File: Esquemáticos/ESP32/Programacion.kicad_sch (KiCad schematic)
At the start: 13 parts, among them J4 USB Programador, U7 ESP32-WROOM-32

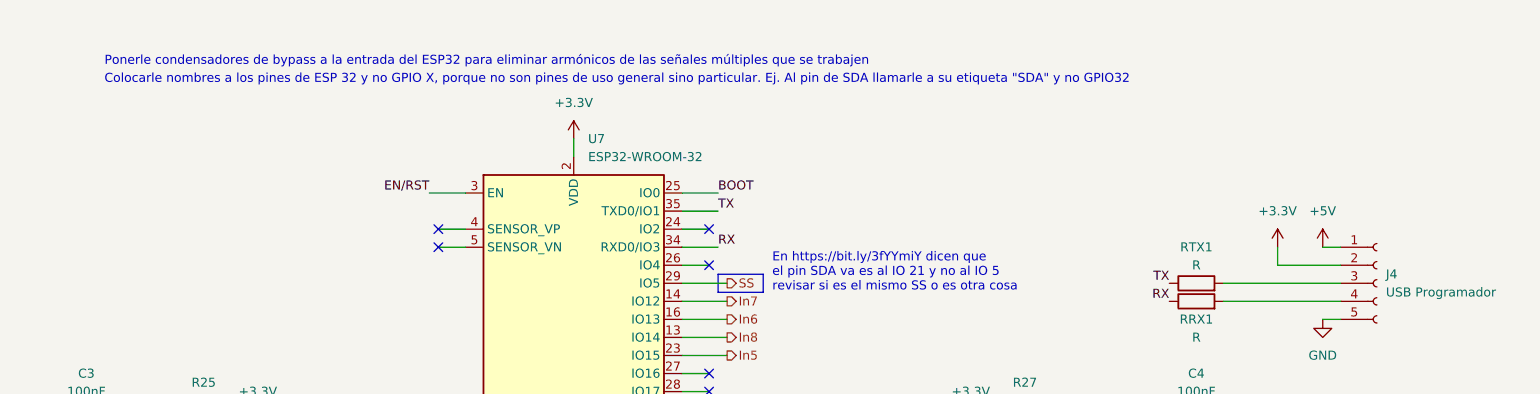
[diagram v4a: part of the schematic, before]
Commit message: Auxilio? Bypass 3.3V ESP32
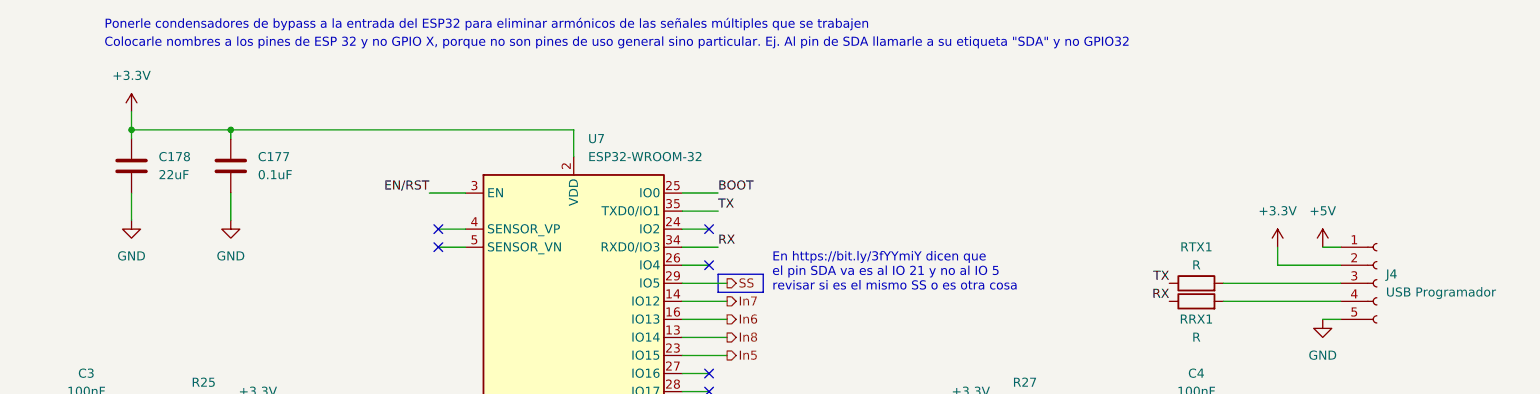
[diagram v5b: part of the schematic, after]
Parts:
- added C177: 0.1uF, Capacitor_SMD:C_0603_1608Metric_Pad1.08x0.95mm_HandSolder, symbol Device:C
- added C178: 22uF, Capacitor_SMD:C_0603_1608Metric_Pad1.08x0.95mm_HandSolder, symbol Device:C
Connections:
- net +3.3V: now also C177.1, C178.1
- net GND: now also C177.2, C178.2
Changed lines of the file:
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@@
   (junction (at 237.49 124.46) (diameter 0) (color 0 0 0 0)
   )
+  (junction (at 80.01 68.58) (diameter 0) (color 0 0 0 0)
+  )
   (junction (at 81.28 124.46) (diameter 0) (color 0 0 0 0)
   )
   (junction (at 66.04 124.46) (diameter 0) (color 0 0 0 0)
+  )
+  (junction (at 93.98 68.58) (diameter 0) (color 0 0 0 0)
   )
   (no_connect (at 123.19 120.65))
@@
     (stroke (width 0) (type default) (color 0 0 0 0))
   )
+  (wire (pts (xy 93.98 68.58) (xy 80.01 68.58))
+    (stroke (width 0) (type default) (color 0 0 0 0))
+  )
   (wire (pts (xy 161.29 133.35) (xy 157.48 133.35))
     (stroke (width 0) (type default) (color 0 0 0 0))
   )
+  (wire (pts (xy 142.24 72.39) (xy 142.24 68.58))
+    (stroke (width 0) (type default) (color 0 0 0 0))
+  )
   (wire (pts (xy 247.65 85.09) (xy 250.19 85.09))
     (stroke (width 0) (type default) (color 0 0 0 0))
@@
     (stroke (width 0) (type default) (color 0 0 0 0))
   )
-  (wire (pts (xy 142.24 69.85) (xy 142.24 72.39))
-    (stroke (width 0) (type default) (color 0 0 0 0))
-  )
   (wire (pts (xy 233.68 90.17) (xy 250.19 90.17))
     (stroke (width 0) (type default) (color 0 0 0 0))
@@
     (stroke (width 0) (type default) (color 0 0 0 0))
   )
+  (wire (pts (xy 80.01 68.58) (xy 80.01 69.85))
+    (stroke (width 0) (type default) (color 0 0 0 0))
+  )
   (wire (pts (xy 241.3 87.63) (xy 250.19 87.63))
     (stroke (width 0) (type default) (color 0 0 0 0))
@@
     (stroke (width 0) (type default) (color 0 0 0 0))
   )
+  (wire (pts (xy 93.98 68.58) (xy 93.98 69.85))
+    (stroke (width 0) (type default) (color 0 0 0 0))
+  )
   (wire (pts (xy 121.92 77.47) (xy 127 77.47))
     (stroke (width 0) (type default) (color 0 0 0 0))
@@
     (stroke (width 0) (type default) (color 0 0 0 0))
   )
+  (wire (pts (xy 80.01 77.47) (xy 80.01 81.28))
+    (stroke (width 0) (type default) (color 0 0 0 0))
+  )
   (wire (pts (xy 157.48 123.19) (xy 163.83 123.19))
     (stroke (width 0) (type default) (color 0 0 0 0))
@@
     (stroke (width 0) (type default) (color 0 0 0 0))
   )
+  (wire (pts (xy 93.98 77.47) (xy 93.98 81.28))
+    (stroke (width 0) (type default) (color 0 0 0 0))
+  )
   (wire (pts (xy 123.19 118.11) (xy 127 118.11))
     (stroke (width 0) (type default) (color 0 0 0 0))
@@
     (stroke (width 0) (type default) (color 0 0 0 0))
   )
+  (wire (pts (xy 142.24 68.58) (xy 93.98 68.58))
+    (stroke (width 0) (type default) (color 0 0 0 0))
+  )
   (wire (pts (xy 161.29 105.41) (xy 157.48 105.41))
     (stroke (width 0) (type default) (color 0 0 0 0))
@@
   )
   (wire (pts (xy 66.04 124.46) (xy 66.04 110.49))
+    (stroke (width 0) (type default) (color 0 0 0 0))
+  )
+  (wire (pts (xy 80.01 66.04) (xy 80.01 68.58))
     (stroke (width 0) (type default) (color 0 0 0 0))
   )
@@
   )
   (text "Ponerle condensadores de bypass a la entrada del ESP32 para eliminar armónicos de las señales múltiples que se trabajen\n"
-    (at 76.2 59.69 0)
+    (at 76.2 54.61 0)
     (effects (font (size 1.27 1.27)) (justify left bottom))
   )
@@
   )
   (text "Colocarle nombres a los pines de ESP 32 y no GPIO X, porque no son pines de uso general sino particular. Ej. Al pin de SDA llamarle a su etiqueta \"SDA\" y no GPIO32"
-    (at 76.2 62.23 0)
+    (at 76.2 57.15 0)
     (effects (font (size 1.27 1.27)) (justify left bottom))
   )
@@
     (pin "2")
   )
+  (symbol (lib_id "Device:C") (at 80.01 73.66 0) (mirror y) (unit 1)
+    (in_bom yes) (on_board yes) (fields_autoplaced)
+    (property "Reference" "C178" (id 0) (at 83.82 72.3899 0)
+      (effects (font (size 1.27 1.27)) (justify right))
+    )
+    (property "Value" "22uF" (id 1) (at 83.82 74.9299 0)
+      (effects (font (size 1.27 1.27)) (justify right))
+    )
+    (property "Footprint" "Capacitor_SMD:C_0603_1608Metric_Pad1.08x0.95mm_HandSolder" (id 2) (at 79.0448 77.47 0)
+      (effects (font (size 1.27 1.27)) hide)
+    )
+    (property "Datasheet" "~" (id 3) (at 80.01 73.66 0)
+      (effects (font (size 1.27 1.27)) hide)
+    )
+    (pin "1")
+    (pin "2")
+  )
   (symbol (lib_id "Device:R") (at 218.44 124.46 270) (mirror x) (unit 1)
     (in_bom yes) (on_board yes) (fields_autoplaced)
@@
     (pin "2")
   )
-  (symbol (lib_id "power:+3.3V") (at 142.24 69.85 0) (unit 1)
-    (in_bom yes) (on_board yes) (fields_autoplaced)
-    (property "Reference" "#PWR030" (id 0) (at 142.24 73.66 0)
-      (effects (font (size 1.27 1.27)) hide)
-    )
-    (property "Value" "+3.3V" (id 1) (at 142.24 64.77 0))
-    (property "Footprint" "" (id 2) (at 142.24 69.85 0)
-      (effects (font (size 1.27 1.27)) hide)
-    )
-    (property "Datasheet" "" (id 3) (at 142.24 69.85 0)
+  (symbol (lib_id "Device:C") (at 93.98 73.66 0) (mirror y) (unit 1)
+    (in_bom yes) (on_board yes) (fields_autoplaced)
+    (property "Reference" "C177" (id 0) (at 97.79 72.3899 0)
+      (effects (font (size 1.27 1.27)) (justify right))
+    )
+    (property "Value" "0.1uF" (id 1) (at 97.79 74.9299 0)
+      (effects (font (size 1.27 1.27)) (justify right))
+    )
+    (property "Footprint" "Capacitor_SMD:C_0603_1608Metric_Pad1.08x0.95mm_HandSolder" (id 2) (at 93.0148 77.47 0)
+      (effects (font (size 1.27 1.27)) hide)
+    )
+    (property "Datasheet" "~" (id 3) (at 93.98 73.66 0)
+      (effects (font (size 1.27 1.27)) hide)
+    )
+    (pin "1")
+    (pin "2")
+  )
+  (symbol (lib_id "power:+3.3V") (at 80.01 66.04 0) (unit 1)
+    (in_bom yes) (on_board yes) (fields_autoplaced)
+    (property "Reference" "#PWR030" (id 0) (at 80.01 69.85 0)
+      (effects (font (size 1.27 1.27)) hide)
+    )
+    (property "Value" "+3.3V" (id 1) (at 80.01 60.96 0))
+    (property "Footprint" "" (id 2) (at 80.01 66.04 0)
+      (effects (font (size 1.27 1.27)) hide)
+    )
+    (property "Datasheet" "" (id 3) (at 80.01 66.04 0)
       (effects (font (size 1.27 1.27)) hide)
     )
@@
     (pin "2")
   )
+  (symbol (lib_id "power:GND") (at 93.98 81.28 0) (unit 1)
+    (in_bom yes) (on_board yes) (fields_autoplaced)
+    (property "Reference" "#PWR0104" (id 0) (at 93.98 87.63 0)
+      (effects (font (size 1.27 1.27)) hide)
+    )
+    (property "Value" "GND" (id 1) (at 93.98 86.36 0))
+    (property "Footprint" "" (id 2) (at 93.98 81.28 0)
+      (effects (font (size 1.27 1.27)) hide)
+    )
+    (property "Datasheet" "" (id 3) (at 93.98 81.28 0)
+      (effects (font (size 1.27 1.27)) hide)
+    )
+    (pin "1")
+  )
   (symbol (lib_id "power:GND") (at 237.49 127 0) (mirror y) (unit 1)
     (in_bom yes) (on_board yes) (fields_autoplaced)
@@
     (pin "2")
   )
+  (symbol (lib_id "power:GND") (at 80.01 81.28 0) (unit 1)
+    (in_bom yes) (on_board yes) (fields_autoplaced)
+    (property "Reference" "#PWR0105" (id 0) (at 80.01 87.63 0)
+      (effects (font (size 1.27 1.27)) hide)
+    )
+    (property "Value" "GND" (id 1) (at 80.01 86.36 0))
+    (property "Footprint" "" (id 2) (at 80.01 81.28 0)
+      (effects (font (size 1.27 1.27)) hide)
+    )
+    (property "Datasheet" "" (id 3) (at 80.01 81.28 0)
+      (effects (font (size 1.27 1.27)) hide)
+    )
+    (pin "1")
+  )
 )

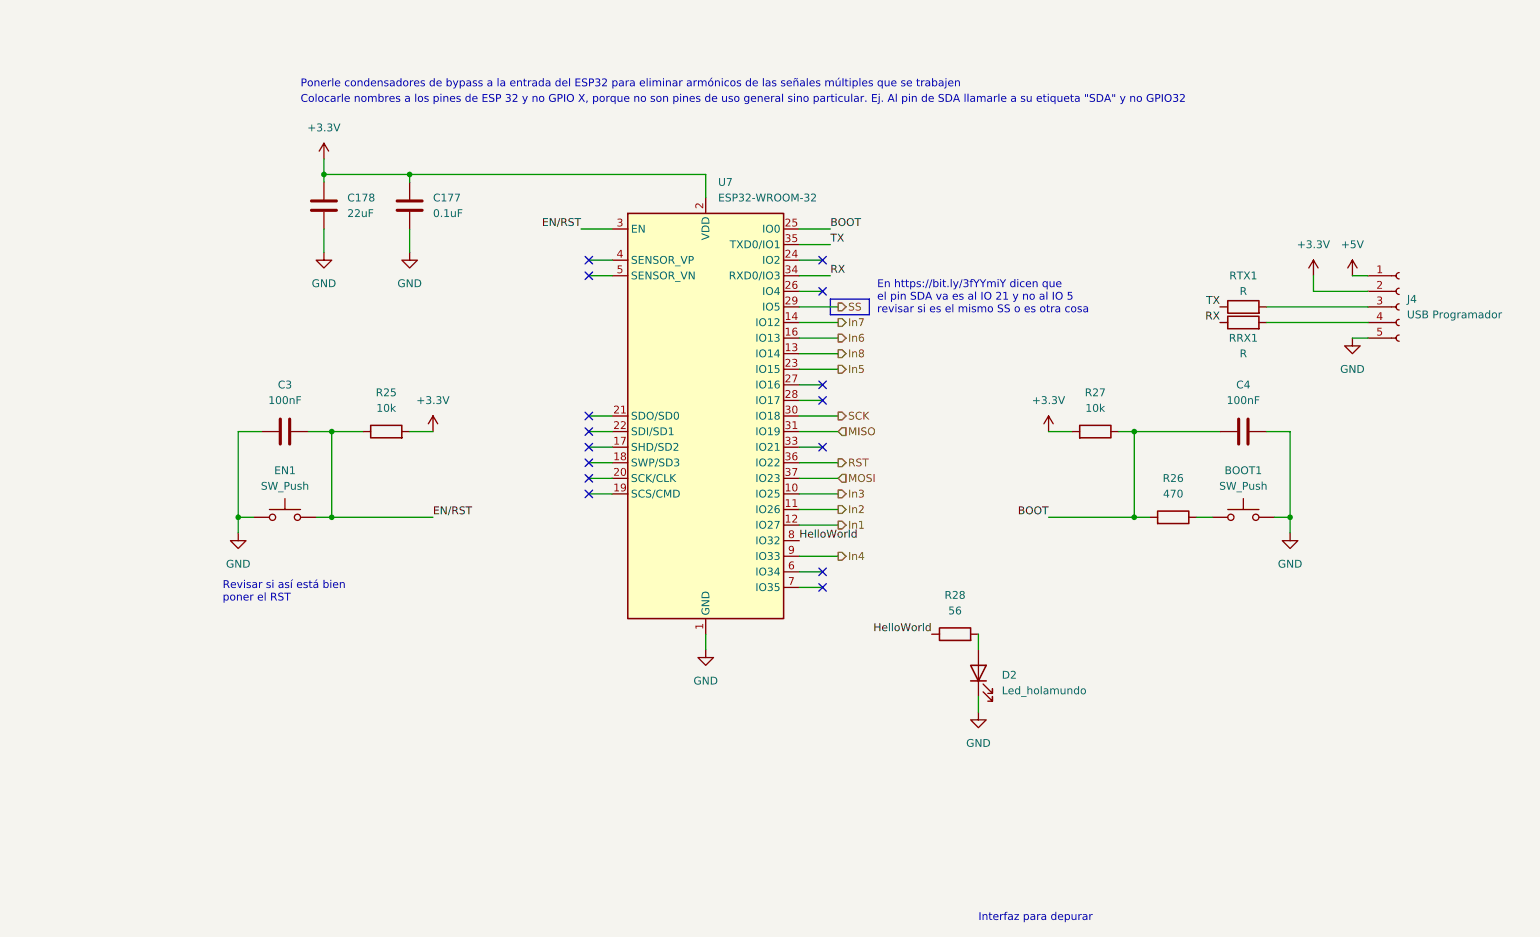
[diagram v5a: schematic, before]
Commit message: Huellas actualizadas según los vendedores locales
Falta la del optoacoplador y actualizar la placa. Además, dependiendo de la resñpuesta del profe tocaría re-diseñar todo :c
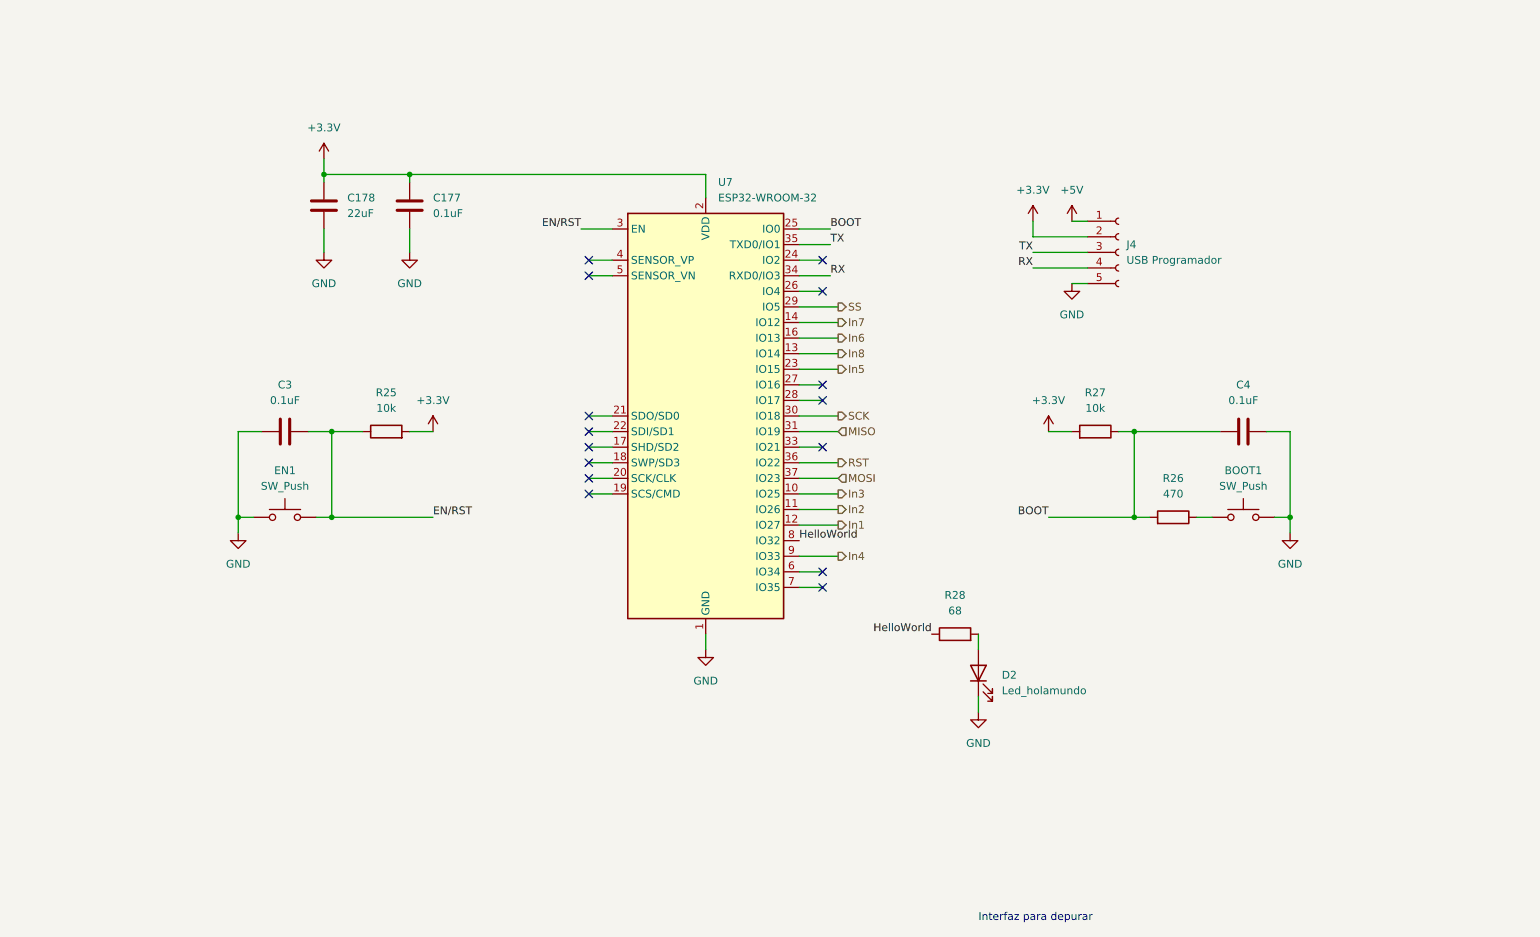
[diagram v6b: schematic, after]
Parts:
- removed RRX1, RTX1: R, Resistor_SMD:R_0603_1608Metric_Pad0.98x0.95mm_HandSolder, symbol Device:R
- BOOT1, EN1: footprint Button_Switch_SMD:SW_SPST_TL3305A -> Button_Switch_SMD:SW_SPST_B3S-1000
- C177, C178: footprint Capacitor_SMD:C_0603_1608Metric_Pad1.08x0.95mm_HandSolder -> Capacitor_SMD:C_0805_2012Metric_Pad1.18x1.45mm_HandSolder
- C3, C4: value 100nF -> 0.1uF; footprint Capacitor_SMD:C_0603_1608Metric_Pad1.08x0.95mm_HandSolder -> Capacitor_SMD:C_0805_2012Metric_Pad1.18x1.45mm_HandSolder
- R25, R26, R27: footprint Resistor_SMD:R_0603_1608Metric_Pad0.98x0.95mm_HandSolder -> Resistor_SMD:R_0805_2012Metric_Pad1.20x1.40mm_HandSolder
- R28: value 56 -> 68; footprint Resistor_SMD:R_0603_1608Metric_Pad0.98x0.95mm_HandSolder -> Resistor_SMD:R_1206_3216Metric_Pad1.30x1.75mm_HandSolder
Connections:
- net RX: now also J4.4 (Pin_4)
- net TX: now also J4.3 (Pin_3)
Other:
- note removed: "Colocarle nombres a los pines de ESP 32 y no GPIO X, porque no son pines de uso general sino particular. Ej. Al pin de SDA llamarle a su etiqueta "SDA" y no GPIO32"
- note removed: "En https://bit.ly/3fYYmiY dicen que el pin SDA va es al IO 21 y no al IO 5 revisar si es el mismo SS o es otra cosa"
- note removed: "Ponerle condensadores de bypass a la entrada del ESP32 para eliminar armónicos de las señales múltiples que se trabajen"
- note removed: "Revisar si así está bien poner el RST"
- moved on the sheet: J4
